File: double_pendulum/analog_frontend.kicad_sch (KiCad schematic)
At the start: 10 parts, among them J5 PJ301M-12, J6 PJ301M-12, J7 Conn_02x10_Odd_Even, U2 TL072, U3 TL072

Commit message: double pendulum 4ms package path update
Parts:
- U2, U3: footprint PCM_4ms_Package_SSOP:TSSOP-8_4.4x3mm_Pitch0.65mm -> 4ms_Package_SSOP:TSSOP-8_4.4x3mm_Pitch0.65mm
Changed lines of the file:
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@@
 			)
 		)
-		(property "Footprint" "PCM_4ms_Package_SSOP:TSSOP-8_4.4x3mm_Pitch0.65mm"
+		(property "Footprint" "4ms_Package_SSOP:TSSOP-8_4.4x3mm_Pitch0.65mm"
 			(at 73.66 68.58 0)
 			(effects
@@
 			)
 		)
-		(property "Footprint" "PCM_4ms_Package_SSOP:TSSOP-8_4.4x3mm_Pitch0.65mm"
+		(property "Footprint" "4ms_Package_SSOP:TSSOP-8_4.4x3mm_Pitch0.65mm"
 			(at 73.66 29.21 0)
 			(effects
@@
 			)
 		)
-		(property "Footprint" "PCM_4ms_Package_SSOP:TSSOP-8_4.4x3mm_Pitch0.65mm"
+		(property "Footprint" "4ms_Package_SSOP:TSSOP-8_4.4x3mm_Pitch0.65mm"
 			(at 72.39 105.41 0)
 			(effects
@@
 			)
 		)
-		(property "Footprint" "PCM_4ms_Package_SSOP:TSSOP-8_4.4x3mm_Pitch0.65mm"
+		(property "Footprint" "4ms_Package_SSOP:TSSOP-8_4.4x3mm_Pitch0.65mm"
 			(at 154.94 63.5 0)
 			(effects

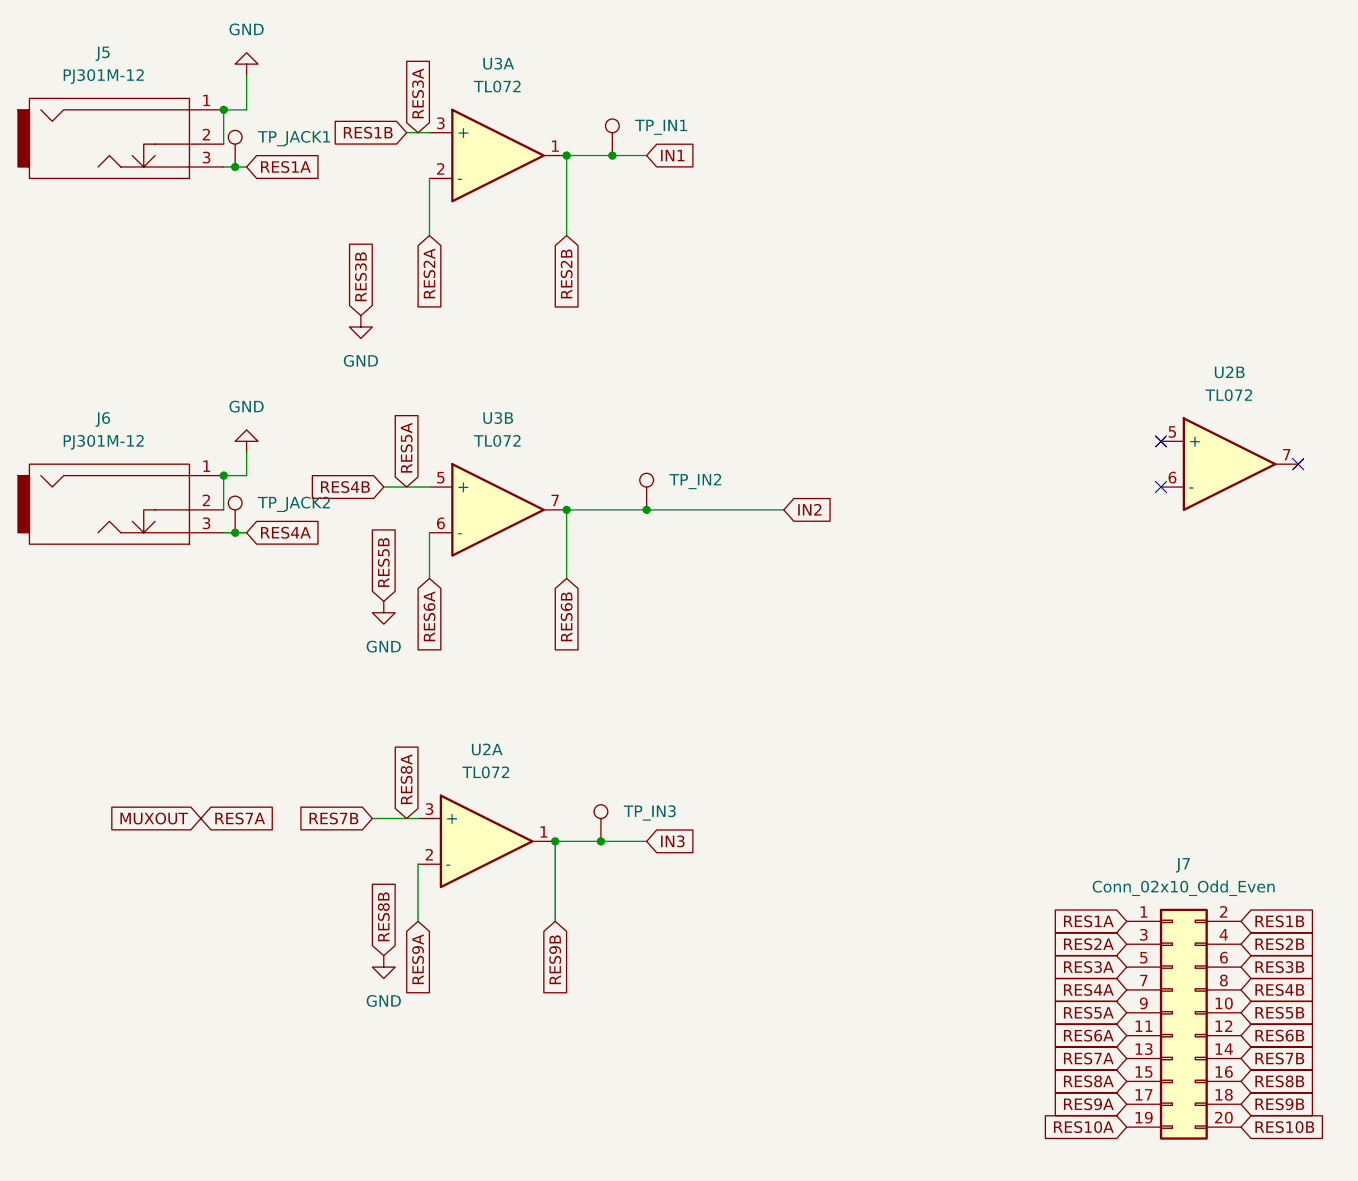
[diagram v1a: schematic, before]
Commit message: Finished schematic and layout of the double pendulum
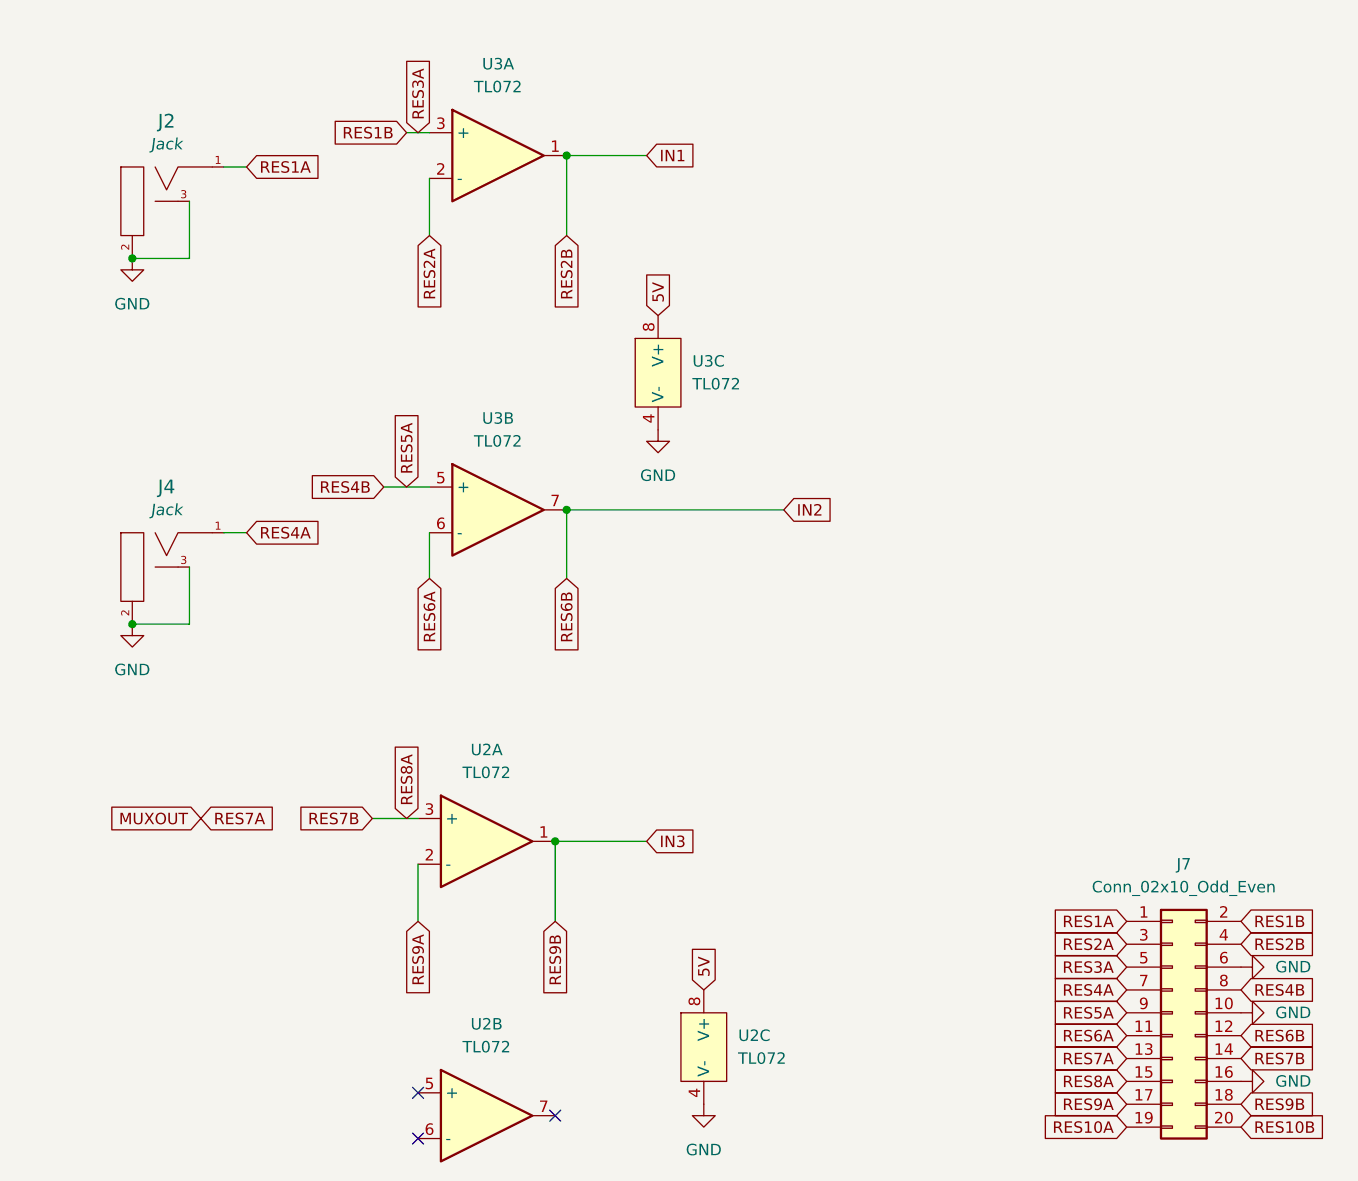
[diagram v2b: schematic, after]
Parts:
- removed J5, J6: PJ301M-12, Eurocad:PJ301M-12, symbol eurocad:PJ301M-12
- removed TP_IN1, TP_IN2, TP_IN3, TP_JACK1, TP_JACK2: TestPoint, TestPoint:TestPoint_Keystone_5005-5009_Compact, symbol Connector:TestPoint
- added J2, J4: 3.5mm_Mono_Switched_sm, 4ms_Jack:EighthInch_PJ398SM, symbol 4ms_Jack:3.5mm_Mono_Switched_sm
- added unit 3 of U2
- added unit 3 of U3
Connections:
- net GND: now also J2.2 (SHEILD), J2.3 (SW), J4.2 (SHEILD), J4.3 (SW), U2.4 (V-), U3.4 (V-)
- net RES1A: now also J2.1 (SIG)
- net RES4A: now also J4.1 (SIG)
- new net 5V: U2.8 (V+), U3.8 (V+)
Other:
- moved on the sheet: U2B
